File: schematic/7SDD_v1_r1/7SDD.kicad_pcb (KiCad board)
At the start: 4 copper layers, 39.4 x 42.9 mm, 43 parts, among them J2 Conn_01x04_Pin, J3 USB_B_Micro, J4 STLINK, SW1 SW_SPDT, U1 AMS1117-3.3, U2 STM32F103C8T6, U3 HDSP-7501, U4 HDSP-7501, U5 HDSP-7501, U7 HDSP-7501, Y1 16 MHz

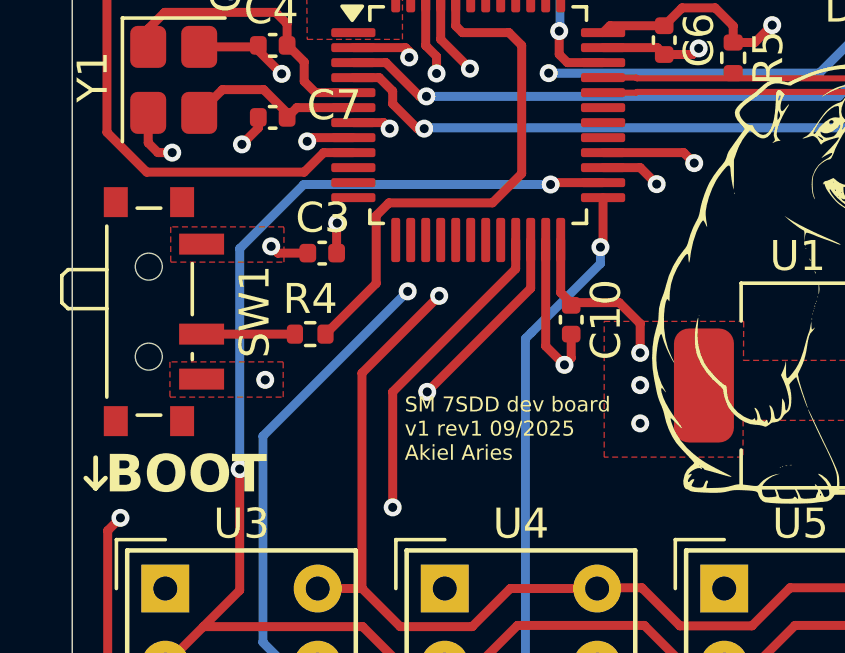
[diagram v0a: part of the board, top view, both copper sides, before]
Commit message: some changes needed for next version based on my recent testing on the new order. biggest issue is FFC connector seems off in routes, INA has bad pinouts?, and LEDs are bright as shit. should probably use bigger resistors on these
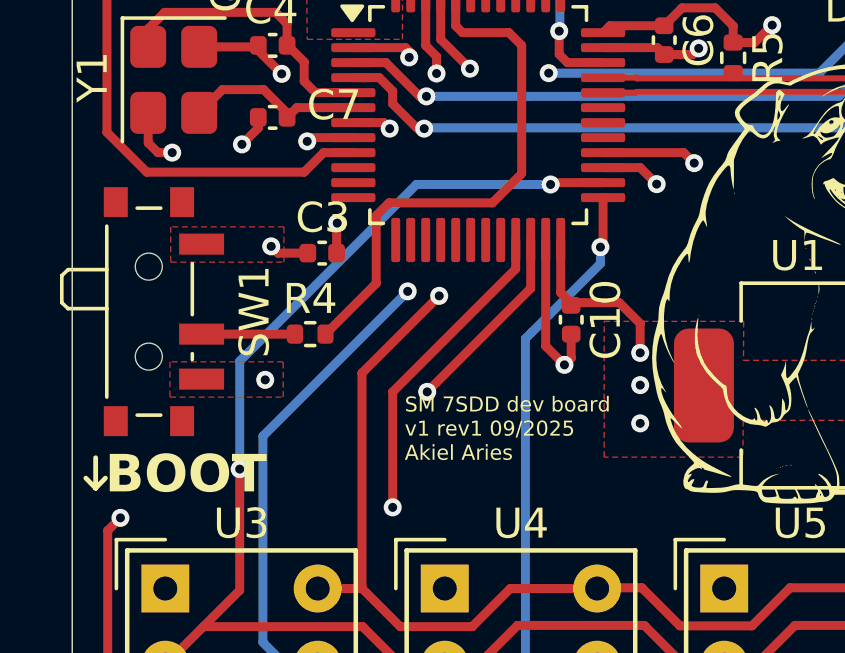
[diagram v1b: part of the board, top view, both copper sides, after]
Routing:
- net /SEG_F: track 57.2 -> 55.0 mm
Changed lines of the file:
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@@
 			(fill yes)
 			(layer "B.SilkS")
-			(net 192260232)
 		)
 		(fp_poly
@@
 			(fill yes)
 			(layer "B.SilkS")
-			(net 192260232)
 		)
 		(fp_poly
@@
 			(fill yes)
 			(layer "B.SilkS")
-			(net 192260232)
 		)
 		(embedded_fonts no)
@@
 	)
 	(segment
-		(start 195.5625 99.4625)
-		(end 187.3375 99.4625)
+		(start 185.2 105.35)
+		(end 185.2 108.925)
 		(width 0.3)
 		(layer "B.Cu")
@@
 	)
 	(segment
-		(start 185.2 101.6)
-		(end 185.2 108.925)
+		(start 191.0875 99.4625)
+		(end 185.2 105.35)
 		(width 0.3)
 		(layer "B.Cu")
@@
 	)
 	(segment
-		(start 187.3375 99.4625)
-		(end 185.2 101.6)
+		(start 195.5625 99.4625)
+		(end 191.0875 99.4625)
 		(width 0.3)
 		(layer "B.Cu")
